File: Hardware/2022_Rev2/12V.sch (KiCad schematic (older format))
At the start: 0 parts

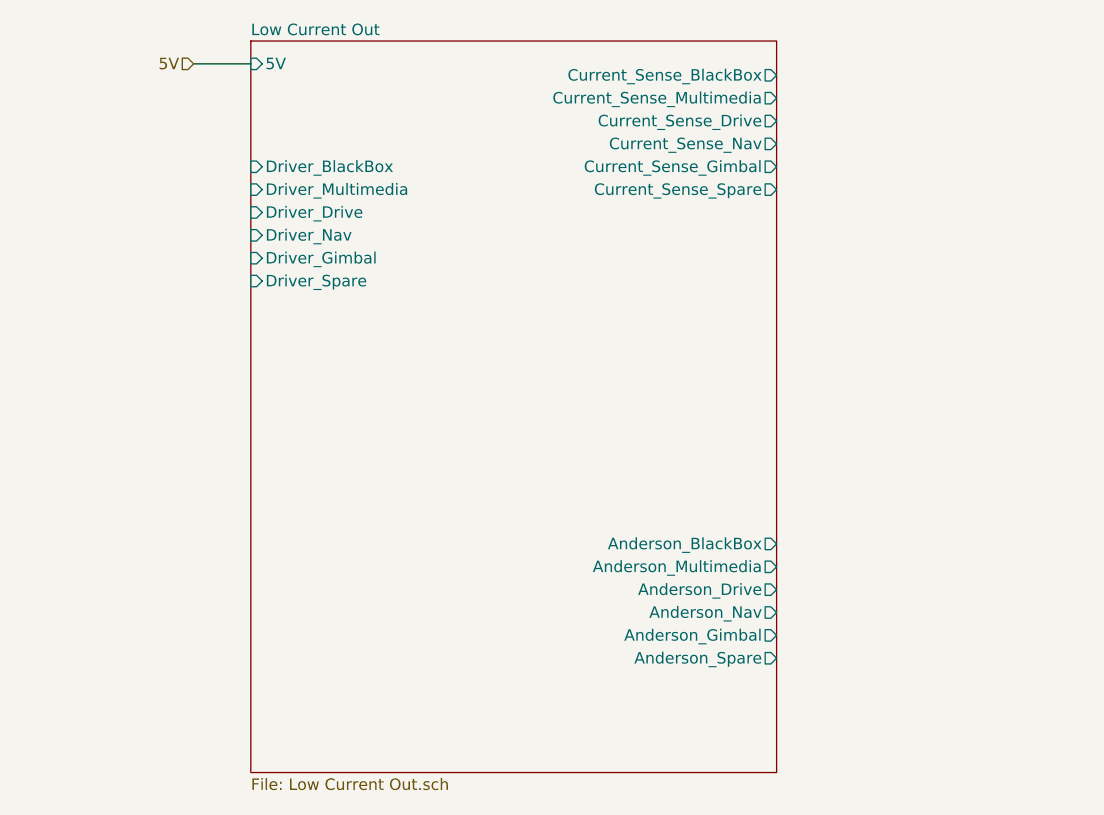
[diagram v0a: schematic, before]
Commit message: Added Heirarchical Labels inside the 12V sheet
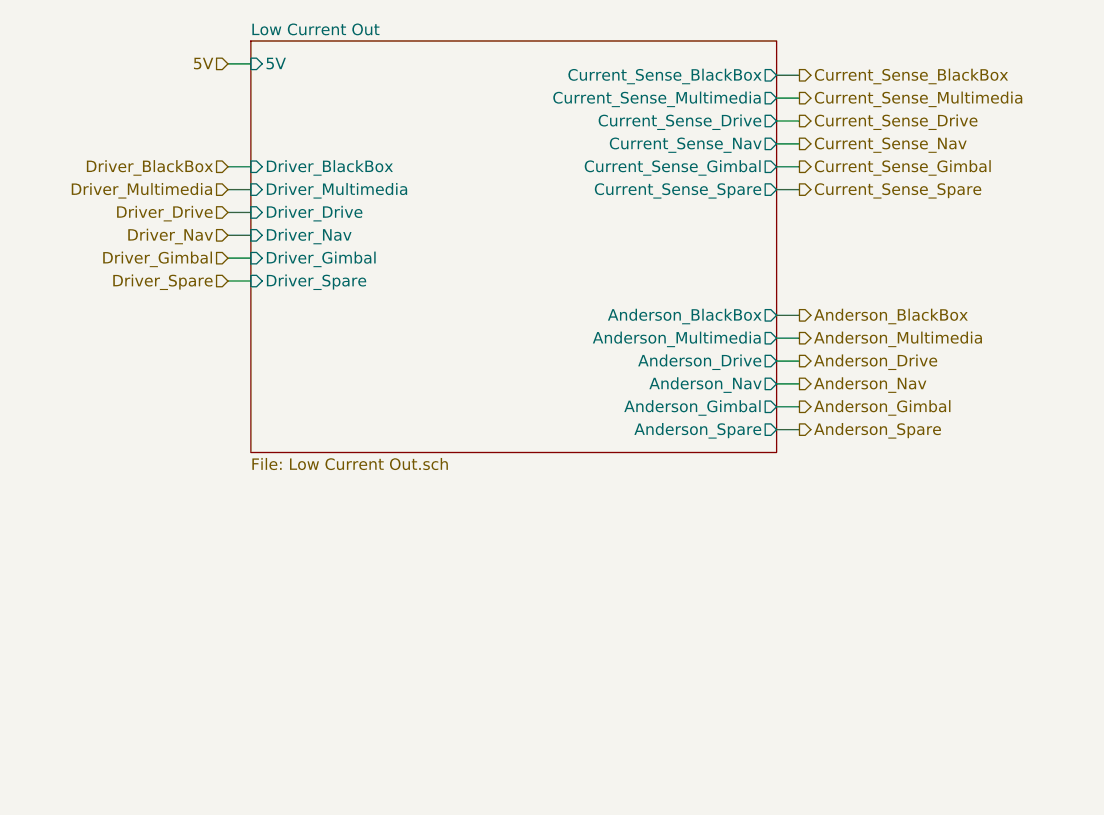
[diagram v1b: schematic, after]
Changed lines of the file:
@@
 $EndDescr
 $Sheet
-S 1350 1150 2300 3200
+S 1350 1150 2300 1800
 U 621219B0
 F0 "Low Current Out" 50
 F1 "Low Current Out.sch" 50
 F2 "Current_Sense_BlackBox" O R 3650 1300 50
-F3 "Anderson_BlackBox" O R 3650 3350 50
+F3 "Anderson_BlackBox" O R 3650 2350 50
 F4 "Driver_BlackBox" I L 1350 1700 50
 F5 "5V" I L 1350 1250 50
 F6 "Current_Sense_Multimedia" O R 3650 1400 50
-F7 "Anderson_Multimedia" O R 3650 3450 50
+F7 "Anderson_Multimedia" O R 3650 2450 50
 F8 "Driver_Multimedia" I L 1350 1800 50
 F9 "Current_Sense_Drive" O R 3650 1500 50
-F10 "Anderson_Drive" O R 3650 3550 50
+F10 "Anderson_Drive" O R 3650 2550 50
 F11 "Driver_Drive" I L 1350 1900 50
 F12 "Current_Sense_Nav" O R 3650 1600 50
-F13 "Anderson_Nav" O R 3650 3650 50
+F13 "Anderson_Nav" O R 3650 2650 50
 F14 "Driver_Nav" I L 1350 2000 50
 F15 "Current_Sense_Gimbal" O R 3650 1700 50
-F16 "Anderson_Gimbal" O R 3650 3750 50
+F16 "Anderson_Gimbal" O R 3650 2750 50
 F17 "Driver_Gimbal" I L 1350 2100 50
 F18 "Current_Sense_Spare" O R 3650 1800 50
-F19 "Anderson_Spare" O R 3650 3850 50
+F19 "Anderson_Spare" O R 3650 2850 50
 F20 "Driver_Spare" I L 1350 2200 50
 $EndSheet
-Text HLabel 1100 1250 0    50   Input ~ 0
+Text HLabel 1250 1250 0    50   Input ~ 0
 5V
+Text HLabel 1250 1700 0    50   Input ~ 0
+Driver_BlackBox
+Text HLabel 1250 1800 0    50   Input ~ 0
+Driver_Multimedia
+Text HLabel 1250 1900 0    50   Input ~ 0
+Driver_Drive
+Text HLabel 1250 2000 0    50   Input ~ 0
+Driver_Nav
+Text HLabel 1250 2100 0    50   Input ~ 0
+Driver_Gimbal
+Text HLabel 1250 2200 0    50   Input ~ 0
+Driver_Spare
 Wire Wire Line
-	1100 1250 1350 1250
+	1250 1250 1350 1250
+Wire Wire Line
+	1250 1700 1350 1700
+Wire Wire Line
+	1350 1800 1250 1800
+Wire Wire Line
+	1250 1900 1350 1900
+Wire Wire Line
+	1350 2000 1250 2000
+Wire Wire Line
+	1250 2100 1350 2100
+Wire Wire Line
+	1350 2200 1250 2200
+Text HLabel 3750 1300 2    50   Output ~ 0
+Current_Sense_BlackBox
+Text HLabel 3750 1400 2    50   Output ~ 0
+Current_Sense_Multimedia
+Text HLabel 3750 1500 2    50   Output ~ 0
+Current_Sense_Drive
+Text HLabel 3750 1600 2    50   Output ~ 0
+Current_Sense_Nav
+Text HLabel 3750 1700 2    50   Output ~ 0
+Current_Sense_Gimbal
+Text HLabel 3750 1800 2    50   Output ~ 0
+Current_Sense_Spare
+Wire Wire Line
+	3750 1800 3650 1800
+Wire Wire Line
+	3650 1700 3750 1700
+Wire Wire Line
+	3750 1600 3650 1600
+Wire Wire Line
+	3650 1500 3750 1500
+Wire Wire Line
+	3750 1400 3650 1400
+Wire Wire Line
+	3650 1300 3750 1300
+Text HLabel 3750 2350 2    50   Output ~ 0
+Anderson_BlackBox
+Text HLabel 3750 2450 2    50   Output ~ 0
+Anderson_Multimedia
+Text HLabel 3750 2550 2    50   Output ~ 0
+Anderson_Drive
+Text HLabel 3750 2650 2    50   Output ~ 0
+Anderson_Nav
+Text HLabel 3750 2750 2    50   Output ~ 0
+Anderson_Gimbal
+Text HLabel 3750 2850 2    50   Output ~ 0
+Anderson_Spare
+Wire Wire Line
+	3750 2350 3650 2350
+Wire Wire Line
+	3650 2450 3750 2450
+Wire Wire Line
+	3750 2550 3650 2550
+Wire Wire Line
+	3650 2650 3750 2650
+Wire Wire Line
+	3750 2750 3650 2750
+Wire Wire Line
+	3650 2850 3750 2850
 $EndSCHEMATC
